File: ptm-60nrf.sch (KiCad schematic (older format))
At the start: 20 parts, among them J1 USB_C_Receptacle_USB2.0, J2 BAT, J3 Conn_01x04_Male, J4 SWD, Q1 AO3407, U1 TP4054, U2 XC6220B331MR-G, U3 nRF52840_holyiot_18010, U4 SRV05-4

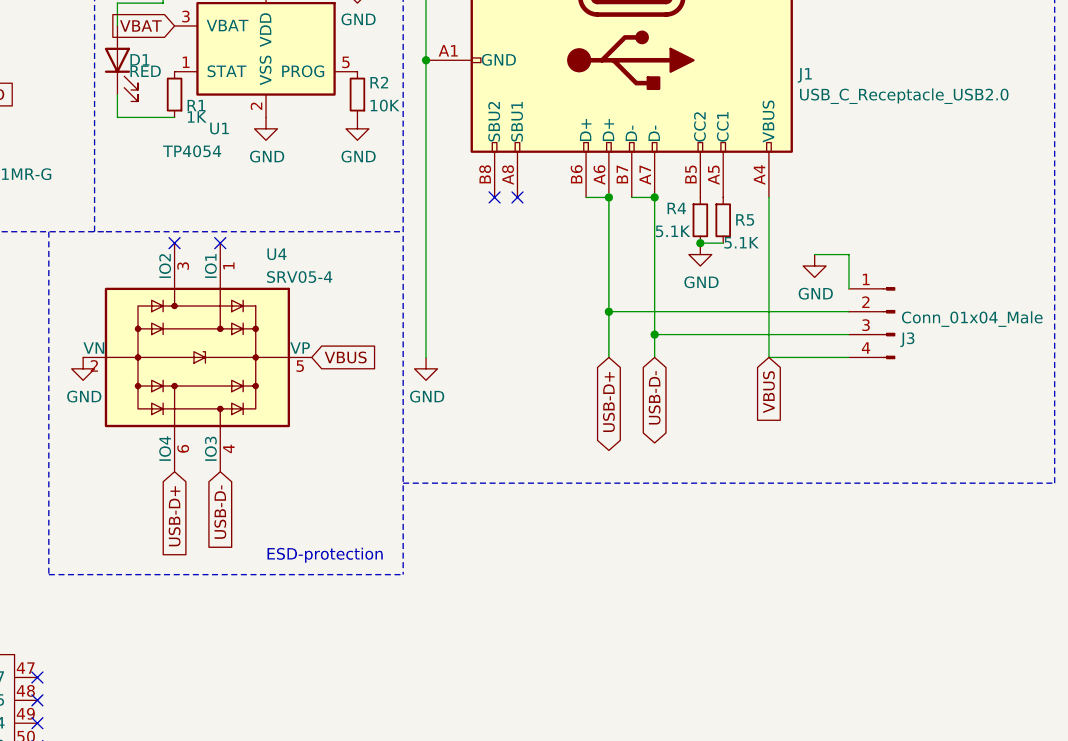
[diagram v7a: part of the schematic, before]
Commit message: swapped switch to pads (savings), added resistor to data
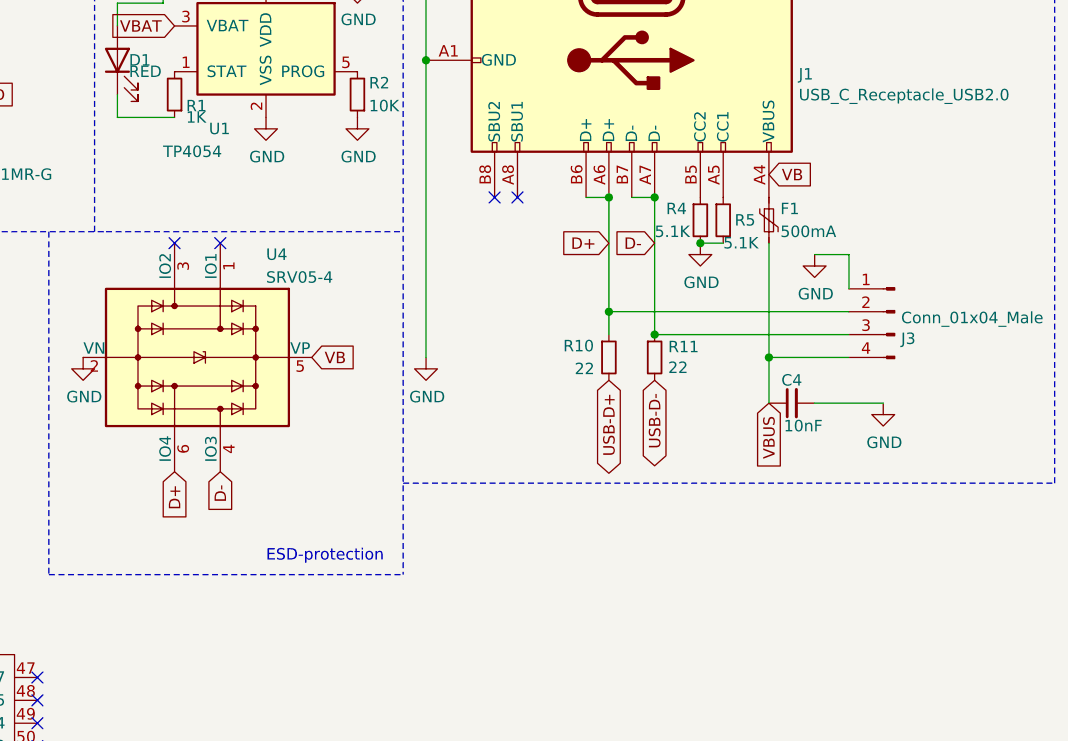
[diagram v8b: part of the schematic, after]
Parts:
- added C4: 10nF, Resistor_SMD:R_0402_1005Metric, symbol Device:C_Small
- added F1: 500mA, Fuse:Fuse_1206_3216Metric, symbol Device:Polyfuse_Small
- added R10, R11: 22, Resistor_SMD:R_0603_1608Metric, symbol Device:R_Small
- Reset1: footprint Button_Switch_SMD:SW_SPST_SKQG_WithStem -> TestPoint:TestPoint_Bridge_Pitch2.0mm_Drill0.7mm; JLCPCB C202424 -> (none)
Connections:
- net GND: now also C4.2
- net USB-D+: now also R10.2; no longer J1.A6 (D+), J1.B6 (D+), J3.2 (Pin_2), U4.6 (IO4)
- net USB-D-: now also R11.2; no longer J1.A7 (D-), J1.B7 (D-), J3.3 (Pin_3), U4.4 (IO3)
- net VBUS: now also C4.1, F1.2; no longer J1.A4 (VBUS), J1.A9 (VBUS), J1.B4 (VBUS), J1.B9 (VBUS), U4.5 (VP)
- new net: F1.1, J1.A4 (VBUS), J1.A9 (VBUS), J1.B4 (VBUS), J1.B9 (VBUS)
- new net D+: J1.A6 (D+), J1.B6 (D+), J3.2 (Pin_2), R10.1, U4.6 (IO4)
- new net D-: J1.A7 (D-), J1.B7 (D-), J3.3 (Pin_3), R11.1, U4.4 (IO3)
- new net VB: U4.5 (VP)
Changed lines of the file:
@@
 	0    1    1    0
 $EndComp
-Text GLabel 6400 2400 3    50   BiDi ~ 0
+Text GLabel 6400 2500 3    50   BiDi ~ 0
 USB-D-
-Text GLabel 6200 2400 3    50   BiDi ~ 0
+Text GLabel 6200 2500 3    50   BiDi ~ 0
 USB-D+
-Text GLabel 6900 2400 3    50   Input ~ 0
+Text GLabel 6900 2600 3    50   Input ~ 0
 VBUS
 $Comp
@@
 F 0 "Reset1" H 8600 2535 50  0000 C CNN
 F 1 "SW_Push" H 8600 2444 50  0000 C CNN
-F 2 "Button_Switch_SMD:SW_SPST_SKQG_WithStem" H 8600 2450 50  0001 C CNN
+F 2 "TestPoint:TestPoint_Bridge_Pitch2.0mm_Drill0.7mm" H 8600 2450 50  0001 C CNN
 F 3 "~" H 8600 2450 50  0001 C CNN
-F 4 "C202424" H 8600 2250 50  0001 C CNN "JLCPCB"
 	1    8600 2250
 	1    0    0    -1
@@
 $EndComp
 Text GLabel 4900 2400 2    50   Input ~ 0
-VBUS
+VB
 $Comp
 L power:GND #PWR0102
@@
 $EndComp
 Text GLabel 4300 2900 3    50   Input ~ 0
-USB-D+
+D+
 Text GLabel 4500 2900 3    50   Input ~ 0
-USB-D-
+D-
 Wire Notes Line width 8
 	2200 1850 4000 1850
@@
 Wire Wire Line
 	6400 1700 6400 2300
-Wire Wire Line
-	6900 1700 6900 2400
 Wire Wire Line
 	3800 5600 3700 5600
@@
 Wire Wire Line
 	6400 2300 7250 2300
-Connection ~ 6400 2300
-Wire Wire Line
-	6400 2300 6400 2400
-Wire Wire Line
-	6200 2200 7250 2200
-Connection ~ 6200 2200
-Wire Wire Line
-	6200 2200 6200 2400
 $Comp
 L power:GND #PWR0105
@@
 Wire Wire Line
 	7250 1950 7100 1950
+$Comp
+L Device:Polyfuse_Small F1
+U 1 1 60CB1404
+P 6900 1800
+F 0 "F1" H 6950 1850 50  0000 L CNN
+F 1 "500mA" H 6950 1750 50  0000 L CNN
+F 2 "Fuse:Fuse_1206_3216Metric" H 6950 1600 50  0001 L CNN
+F 3 "~" H 6900 1800 50  0001 C CNN
+F 4 "C70069" H 6900 1800 50  0001 C CNN "JLCPCB"
+	1    6900 1800
+	1    0    0    -1
+$EndComp
+$Comp
+L Device:R_Small R11
+U 1 1 60CB30A9
+P 6400 2400
+F 0 "R11" H 6459 2446 50  0000 L CNN
+F 1 "22" H 6459 2355 50  0000 L CNN
+F 2 "Resistor_SMD:R_0603_1608Metric" H 6400 2400 50  0001 C CNN
+F 3 "~" H 6400 2400 50  0001 C CNN
+	1    6400 2400
+	1    0    0    -1
+$EndComp
+Connection ~ 6400 2300
+$Comp
+L Device:R_Small R10
+U 1 1 60CB3411
+P 6200 2400
+F 0 "R10" H 6000 2450 50  0000 L CNN
+F 1 "22" H 6050 2350 50  0000 L CNN
+F 2 "Resistor_SMD:R_0603_1608Metric" H 6200 2400 50  0001 C CNN
+F 3 "~" H 6200 2400 50  0001 C CNN
+	1    6200 2400
+	1    0    0    -1
+$EndComp
+Wire Wire Line
+	6200 2200 6200 2300
+Connection ~ 6200 2200
+Wire Wire Line
+	6200 2200 7250 2200
+Connection ~ 6900 2400
+Wire Wire Line
+	6900 2400 6900 2600
+Wire Wire Line
+	6900 1900 6900 2400
+$Comp
+L Device:C_Small C4
+U 1 1 60CE239C
+P 7000 2600
+F 0 "C4" V 7100 2600 50  0000 C CNN
+F 1 "10nF" V 6900 2550 50  0000 C CNN
+F 2 "Resistor_SMD:R_0402_1005Metric" H 7000 2600 50  0001 C CNN
+F 3 "~" H 7000 2600 50  0001 C CNN
+F 4 "C15195" V 7000 2600 50  0001 C CNN "JLCPCB"
+	1    7000 2600
+	0    -1   -1   0
+$EndComp
+$Comp
+L power:GND #PWR0106
+U 1 1 60CE461E
+P 7400 2600
+F 0 "#PWR0106" H 7400 2350 50  0001 C CNN
+F 1 "GND" H 7405 2427 50  0000 C CNN
+F 2 "" H 7400 2600 50  0001 C CNN
+F 3 "" H 7400 2600 50  0001 C CNN
+	1    7400 2600
+	1    0    0    -1
+$EndComp
+Wire Wire Line
+	7400 2600 7100 2600
+Text GLabel 6200 1900 0    50   Input ~ 0
+D+
+Text GLabel 6400 1900 0    50   Input ~ 0
+D-
+Text GLabel 6900 1600 2    50   Input ~ 0
+VB
 $EndSCHEMATC
